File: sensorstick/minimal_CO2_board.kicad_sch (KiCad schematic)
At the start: 4 parts, among them J1 USB_A, U1 ESP32-C3_SUPERMINI

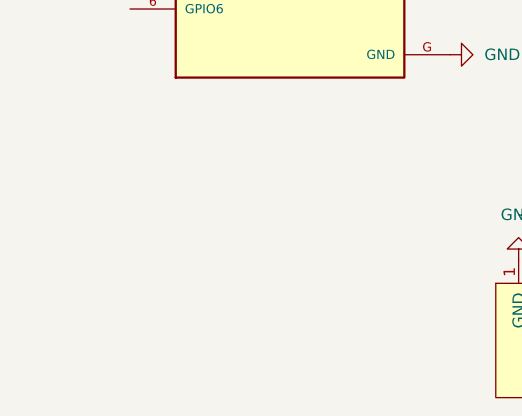
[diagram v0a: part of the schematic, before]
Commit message: add battery
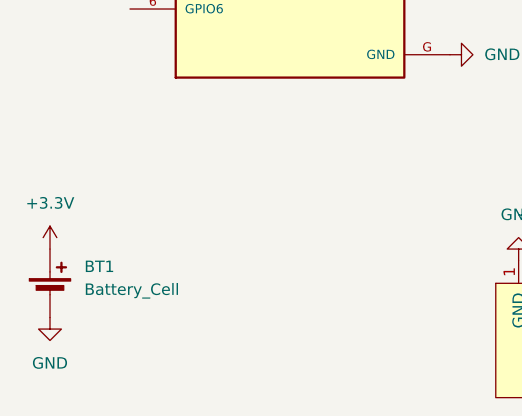
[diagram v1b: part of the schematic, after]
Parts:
- added BT1: Battery_Cell, CustomLibrary:BatteryHolder_Keystone_1060_1x2032, symbol Device:Battery_Cell
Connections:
- net +3.3V: now also BT1.1 (+)
- net GND: now also BT1.2 (-)
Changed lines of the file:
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@@
+	)
+	(symbol
+		(lib_id "power:GND")
+		(at 36.83 97.79 0)
+		(unit 1)
+		(exclude_from_sim no)
+		(in_bom yes)
+		(on_board yes)
+		(dnp no)
+		(fields_autoplaced yes)
+		(property "Reference" "#PWR011"
+			(at 36.83 104.14 0)
+			(effects
+				(font
+					(size 1.27 1.27)
+				)
+				(hide yes)
+			)
+		)
+		(property "Value" "GND"
+			(at 36.83 102.87 0)
+			(effects
+				(font
+					(size 1.27 1.27)
+				)
+			)
+		)
+		(property "Footprint" ""
+			(at 36.83 97.79 0)
+			(effects
+				(font
+					(size 1.27 1.27)
+				)
+				(hide yes)
+			)
+		)
+		(property "Datasheet" ""
+			(at 36.83 97.79 0)
+			(effects
+				(font
+					(size 1.27 1.27)
+				)
+				(hide yes)
+			)
+		)
+		(property "Description" "Power symbol creates a global label with name \"GND\" , ground"
+			(at 36.83 97.79 0)
+			(effects
+				(font
+					(size 1.27 1.27)
+				)
+				(hide yes)
+			)
+		)
+		(pin "1"
+		)
+		(instances
+			(project ""
+				(path "/7be59ae3-cff4-4640-882e-dfffcfbe988a"
+					(reference "#PWR011")
+					(unit 1)
+				)
+			)
+		)
 	)
 	(symbol
@@
 	)
 	(symbol
+		(lib_id "Device:Battery_Cell")
+		(at 36.83 95.25 0)
+		(unit 1)
+		(exclude_from_sim no)
+		(in_bom yes)
+		(on_board yes)
+		(dnp no)
+		(fields_autoplaced yes)
+		(property "Reference" "BT1"
+			(at 40.64 92.1384 0)
+			(effects
+				(font
+					(size 1.27 1.27)
+				)
+				(justify left)
+			)
+		)
+		(property "Value" "Battery_Cell"
+			(at 40.64 94.6784 0)
+			(effects
+				(font
+					(size 1.27 1.27)
+				)
+				(justify left)
+			)
+		)
+		(property "Footprint" "CustomLibrary:BatteryHolder_Keystone_1060_1x2032"
+			(at 36.83 93.726 90)
+			(effects
+				(font
+					(size 1.27 1.27)
+				)
+				(hide yes)
+			)
+		)
+		(property "Datasheet" "~"
+			(at 36.83 93.726 90)
+			(effects
+				(font
+					(size 1.27 1.27)
+				)
+				(hide yes)
+			)
+		)
+		(property "Description" "Single-cell battery"
+			(at 36.83 95.25 0)
+			(effects
+				(font
+					(size 1.27 1.27)
+				)
+				(hide yes)
+			)
+		)
+		(pin "2"
+		)
+		(pin "1"
+		)
+		(instances
+			(project ""
+				(path "/7be59ae3-cff4-4640-882e-dfffcfbe988a"
+					(reference "BT1")
+					(unit 1)
+				)
+			)
+		)
+	)
+	(symbol
 		(lib_id "CustomSymbols:SSD1306")
 		(at 92.71 100.33 0)
@@
 					(unit 1)
 				)
+			)
+		)
+	)
+	(symbol
+		(lib_id "power:+3.3V")
+		(at 36.83 90.17 0)
+		(unit 1)
+		(exclude_from_sim no)
+		(in_bom yes)
+		(on_board yes)
+		(dnp no)
+		(fields_autoplaced yes)
+		(property "Reference" "#PWR010"
+			(at 36.83 93.98 0)
+			(effects
+				(font
+					(size 1.27 1.27)
+				)
+				(hide yes)
+			)
+		)
+		(property "Value" "+3.3V"
+			(at 36.83 85.09 0)
+			(effects
+				(font
+					(size 1.27 1.27)
+				)
+			)
+		)
+		(property "Footprint" ""
+			(at 36.83 90.17 0)
+			(effects
+				(font
+					(size 1.27 1.27)
+				)
+				(hide yes)
+			)
+		)
+		(property "Datasheet" ""
+			(at 36.83 90.17 0)
+			(effects
+				(font
+					(size 1.27 1.27)
+				)
+				(hide yes)
+			)
+		)
+		(property "Description" "Power symbol creates a global label with name \"+3.3V\""
+			(at 36.83 90.17 0)
+			(effects
+				(font
+					(size 1.27 1.27)
+				)
+				(hide yes)
+			)
+		)
+		(pin "1"
+		)
+		(instances
+			(project ""
+				(path "/7be59ae3-cff4-4640-882e-dfffcfbe988a"
+					(reference "#PWR010")
+					(unit 1)
+				)

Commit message: add stuff
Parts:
- removed Brd1: SSD1306, CustomLibrary:128x64OLED, symbol CustomSymbols:SSD1306
- removed J1: USB_A, Connector_USB:USB_A_CNCTech_1001-011-01101_Horizontal, symbol Connector:USB_A
- added OLED1: HS91L02W2C01, CustomLibrary:OLED-TH_L38.0-W12.0_HS91L02W2C01, symbol CustomSymbols:HS91L02W2C01
- added USB1: U217-04XN-XXR84, CustomLibrary:USB-A-SMD_U217-041N-4BV81, symbol CustomSymbols:U217-04XN-XXR84
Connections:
- net +3.3V: now also USB1.1 (VCC)
- net +5V: now also OLED1.2 (VCC)
- net GND: now also OLED1.1 (GND), USB1.4 (GND)
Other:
- moved on the sheet: BT1, U2
